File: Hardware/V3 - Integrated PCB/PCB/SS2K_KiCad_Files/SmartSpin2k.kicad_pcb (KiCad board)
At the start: 2 copper layers, 57.2 x 60.3 mm, 84 parts, among them J1 B4B-XH-AMLFSN, J2 B4B-XH-AMLFSN, J3 B8B-XH-A_LFSN, J4 10118194-0001LF, Q1 S8050, Q2 S8050, SW1 SW_Push, SW2 SW_Push, U1 ESP32-WROOM-32D, U2 TMC2209-LA-T, U3 MAX3232, U4 TPS5430DDA, U5 INTERFACE-CP2102-GMR(QFN28), U6 LM1117-3.3

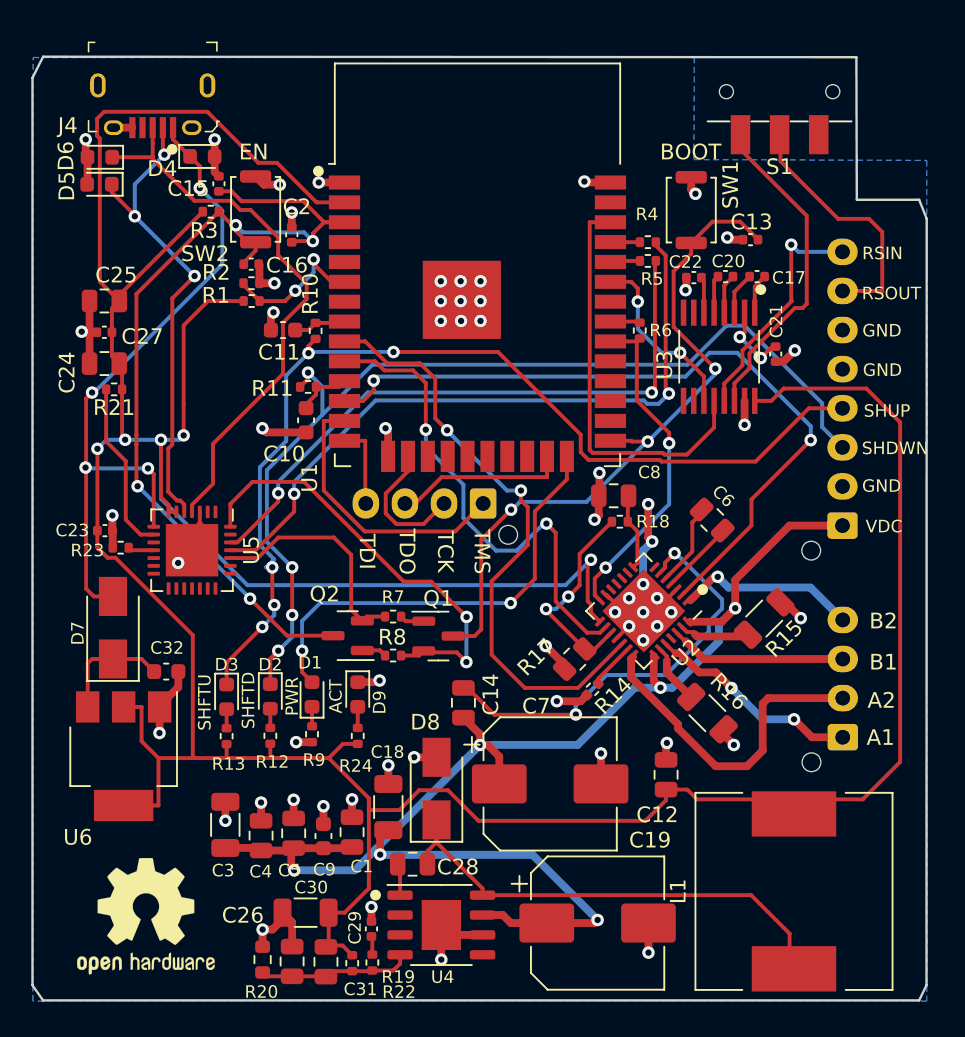
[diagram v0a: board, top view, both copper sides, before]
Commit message: PCB Changes
Made edges perfectly horizontal and vertical.
Changed switch part number
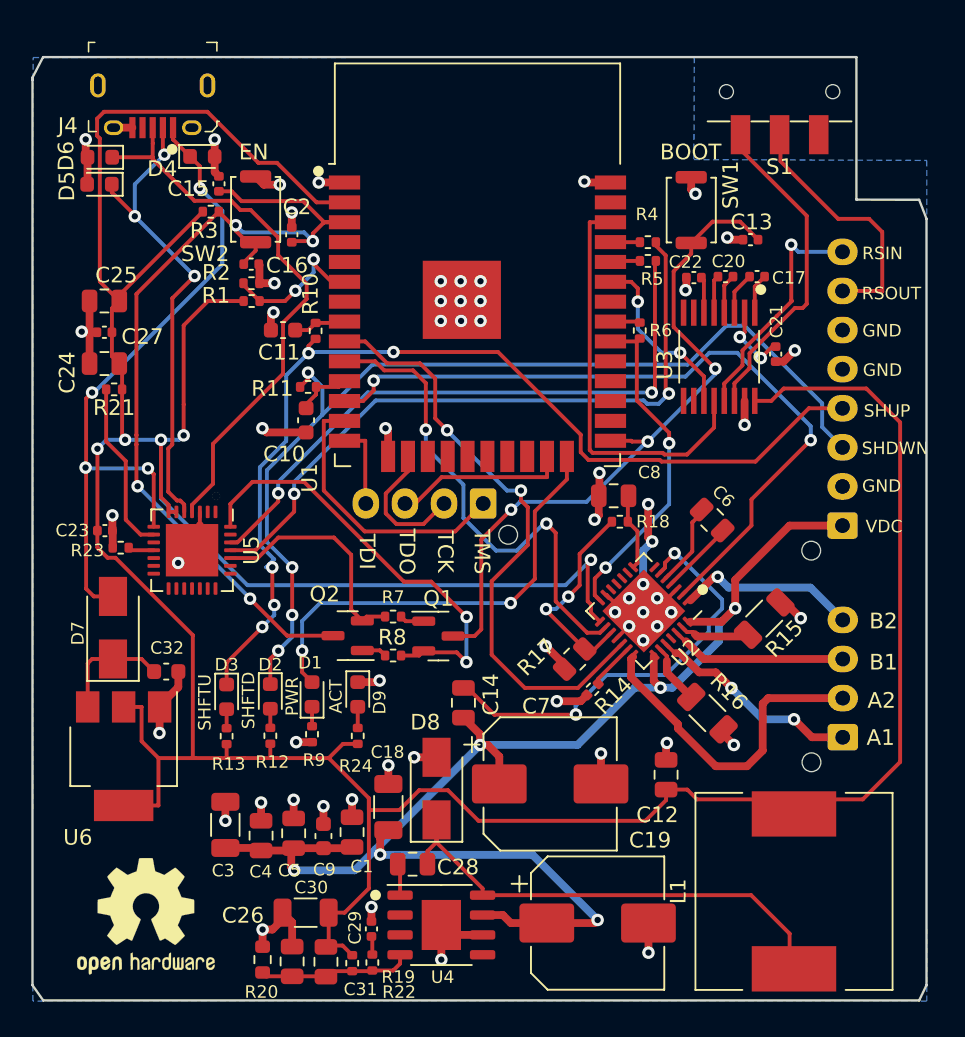
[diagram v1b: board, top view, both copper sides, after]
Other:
- outline, holes or cut-outs redrawn
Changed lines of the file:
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@@
   (gr_line (start 122.72 89.645) (end 122.72 147.97) (layer "Dwgs.User") (width 0.15))
   (gr_line (start 177.07 98.044) (end 177.07 147.97) (layer "Dwgs.User") (width 0.15))
-  (gr_line (start 122 148.97) (end 178 148.97) (layer "Edge.Cuts") (width 0.15))
-  (gr_line (start 122 88.645) (end 121.32 90) (layer "Edge.Cuts") (width 0.15))
-  (gr_line (start 174.0154 97.789825) (end 173.988 88.678288) (layer "Edge.Cuts") (width 0.15))
-  (gr_line (start 173.988 88.678288) (end 122 88.645) (layer "Edge.Cuts") (width 0.15))
-  (gr_line (start 121.32 90) (end 121.32 148) (layer "Edge.Cuts") (width 0.15))
-  (gr_line (start 174.0154 97.789825) (end 178 97.79) (layer "Edge.Cuts") (width 0.15))
-  (gr_line (start 121.32 148) (end 122 148.97) (layer "Edge.Cuts") (width 0.15))
+  (gr_line (start 122.01 148.97) (end 178 148.97) (layer "Edge.Cuts") (width 0.15))
+  (gr_line (start 122 88.67) (end 121.32 89.98) (layer "Edge.Cuts") (width 0.15))
+  (gr_line (start 173.988 97.781537) (end 173.988 88.67) (layer "Edge.Cuts") (width 0.15))
+  (gr_line (start 173.988 88.67) (end 122 88.67) (layer "Edge.Cuts") (width 0.15))
+  (gr_line (start 121.32 89.98) (end 121.32 90.14) (layer "Edge.Cuts") (width 0.15))
+  (gr_line (start 121.32 90.14) (end 121.32 148) (layer "Edge.Cuts") (width 0.15))
+  (gr_line (start 173.988 97.781537) (end 178 97.79) (layer "Edge.Cuts") (width 0.15))
+  (gr_line (start 121.32 148) (end 122.01 148.97) (layer "Edge.Cuts") (width 0.15))
+  (gr_line (start 178.47 148) (end 178.47 148) (layer "Edge.Cuts") (width 0.15))
   (gr_line (start 178.47 148) (end 178 148.97) (layer "Edge.Cuts") (width 0.15))
-  (gr_line (start 178.4826 99) (end 178 97.79) (layer "Edge.Cuts") (width 0.15))
-  (gr_line (start 178.4826 99) (end 178.47 148) (layer "Edge.Cuts") (width 0.15))
+  (gr_line (start 178.47 99) (end 178 97.79) (layer "Edge.Cuts") (width 0.15))
+  (gr_line (start 178.47 99) (end 178.47 148) (layer "Edge.Cuts") (width 0.15))
   (gr_text "B1" (at 168.57 127.33) (layer "B.SilkS")
     (effects (font (size 0.8 0.8) (thickness 0.1)) (justify mirror))

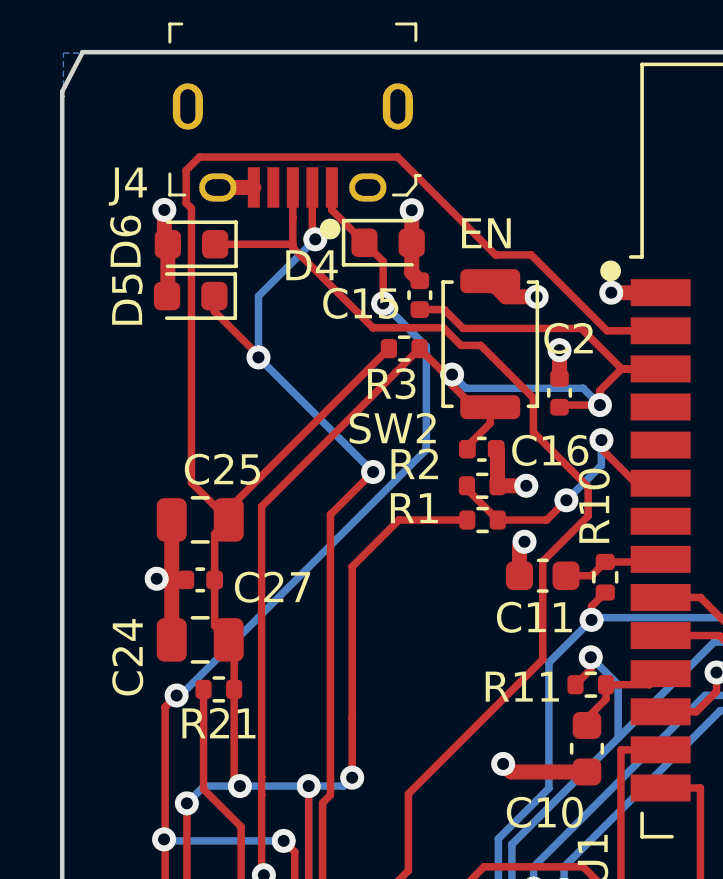
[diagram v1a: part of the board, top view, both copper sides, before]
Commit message: Switched to TVS IC instead of individuals
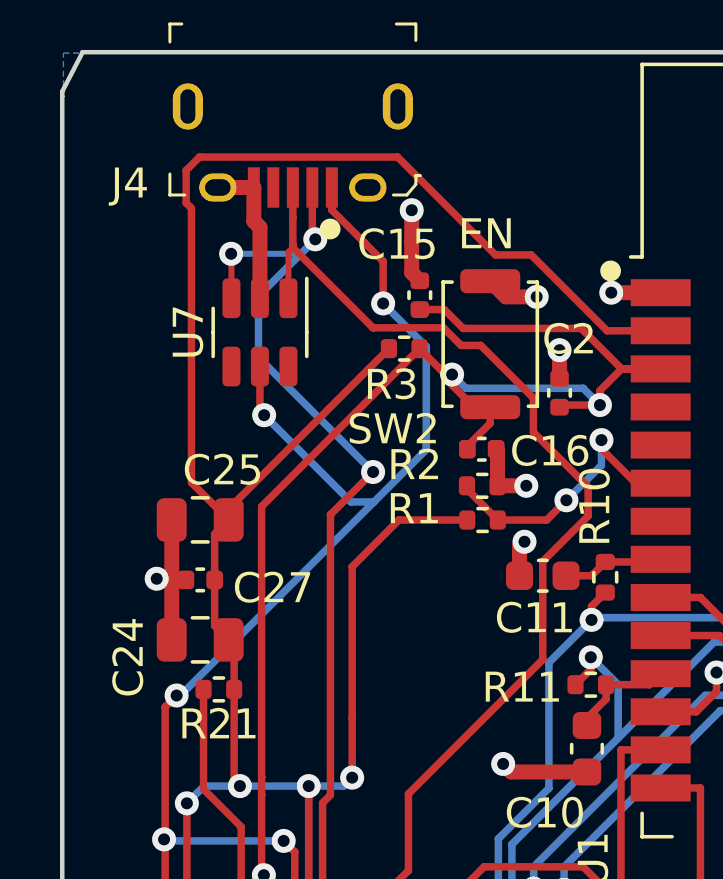
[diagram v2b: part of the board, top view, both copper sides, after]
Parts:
- removed D4, D5, D6: D_TVS, Diode_SMD:D_0603_1608Metric
- added U7: SRV05-4, Package_TO_SOT_SMD:SOT-23-6, F.Cu at (127.9, 98.0)
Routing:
- net /VBUS: track 44.3 -> 50.8 mm, vias 4 -> 5
- net /D-: track 30.9 -> 32.7 mm
- net GND: track 90.5 -> 91.3 mm, vias 60 -> 59
- net /D+: track 36.0 -> 35.2 mm
